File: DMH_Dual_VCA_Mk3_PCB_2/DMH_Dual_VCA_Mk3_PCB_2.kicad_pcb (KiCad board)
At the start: 2 copper layers, 48 x 175 mm, 78 parts, among them J1 TS_Jack_6.35mm_Sw, J100 IDC_02x05, J2 TS_Jack_6.35mm_Sw, J200 IDC_02x05, J3 TS_Jack_6.35mm_Sw, J4 TS_Jack_6.35mm_Sw, J5 TS_Jack_6.35mm_Sw, J50 Conn_01x08, J6 TS_Jack_6.35mm_Sw, J60 Conn_01x08, J7 TS_Jack_6.35mm_Sw, J8 TS_Jack_6.35mm_Sw, J9 TS_Jack_6.35mm_Sw, Q1 BC548, Q2 BC548, Q3 BC548, Q4 BC548, U1 TL074, U2 TL074, U3 TL072

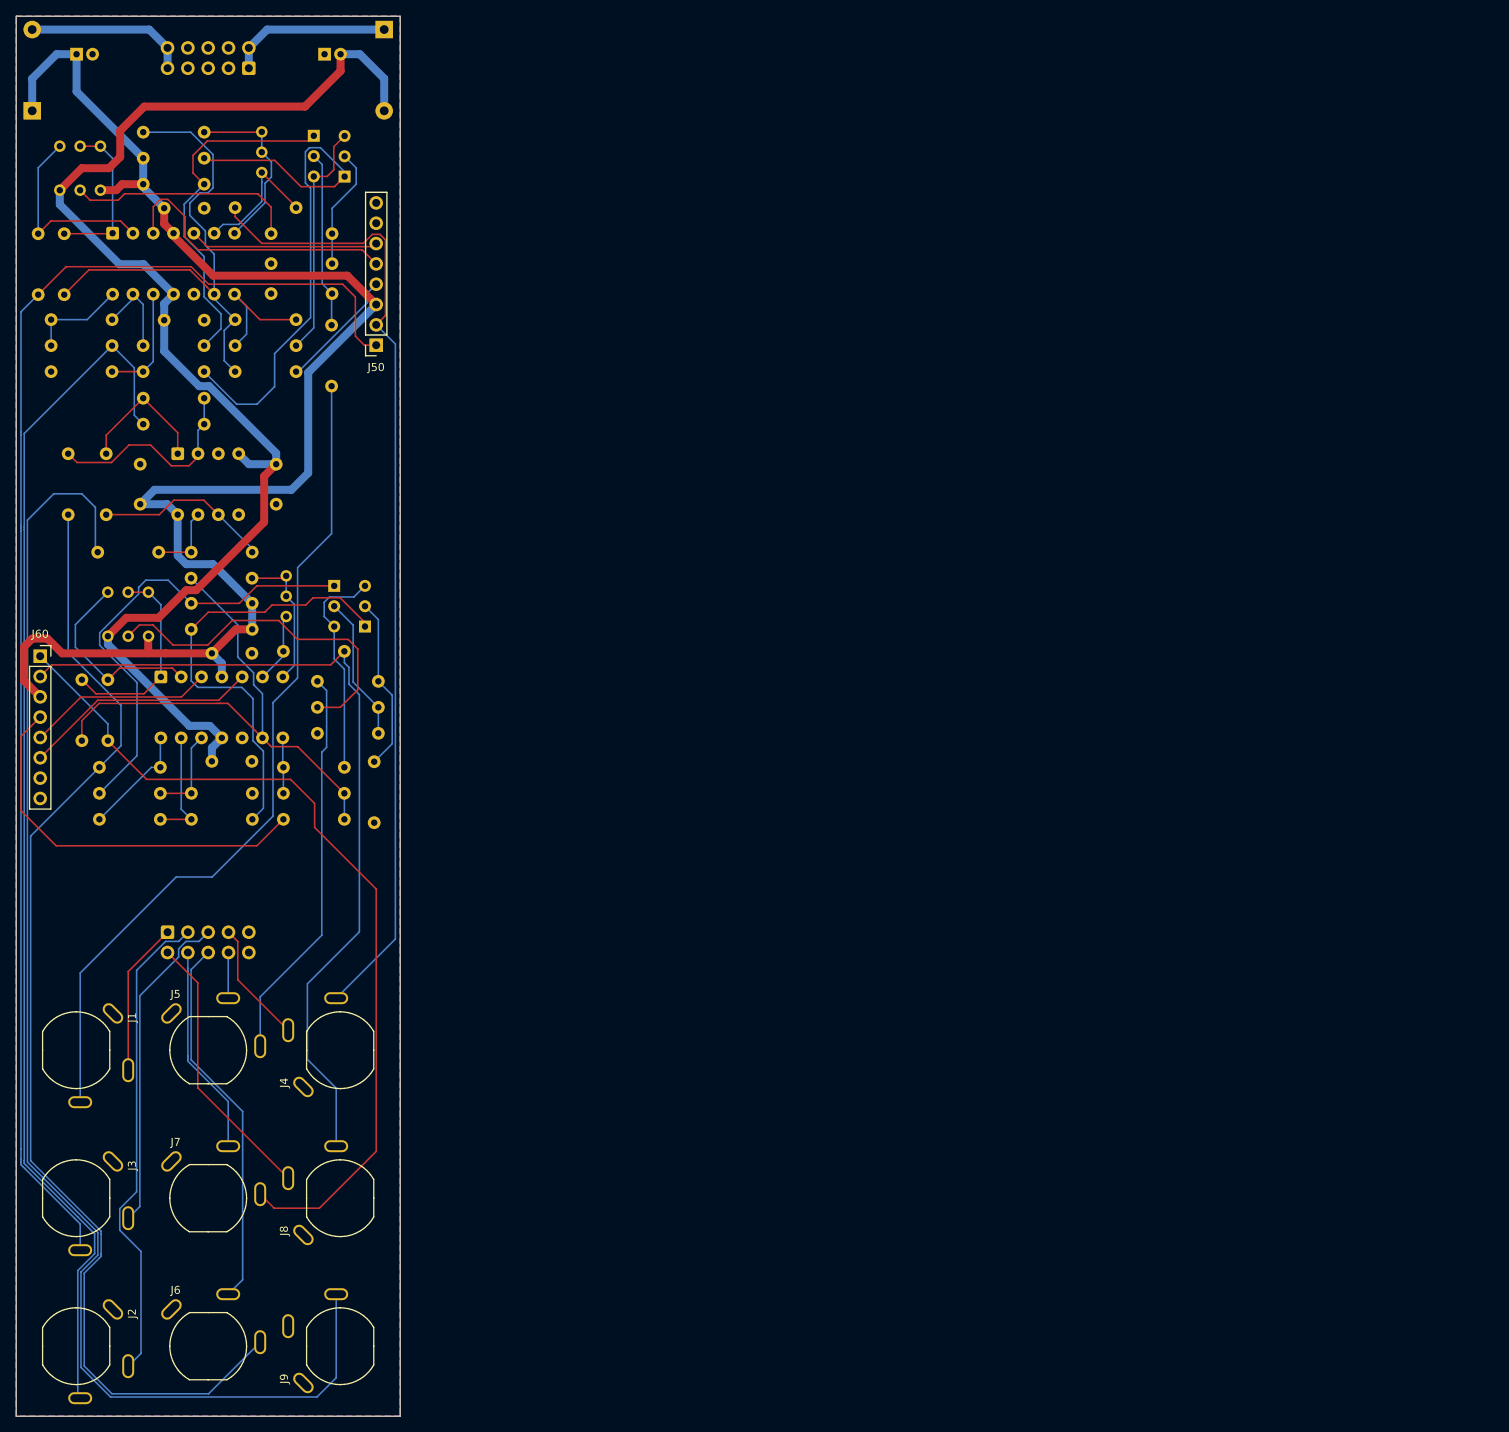
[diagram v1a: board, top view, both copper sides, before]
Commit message: Added clipping LED to schematic
Still need to add to Panel
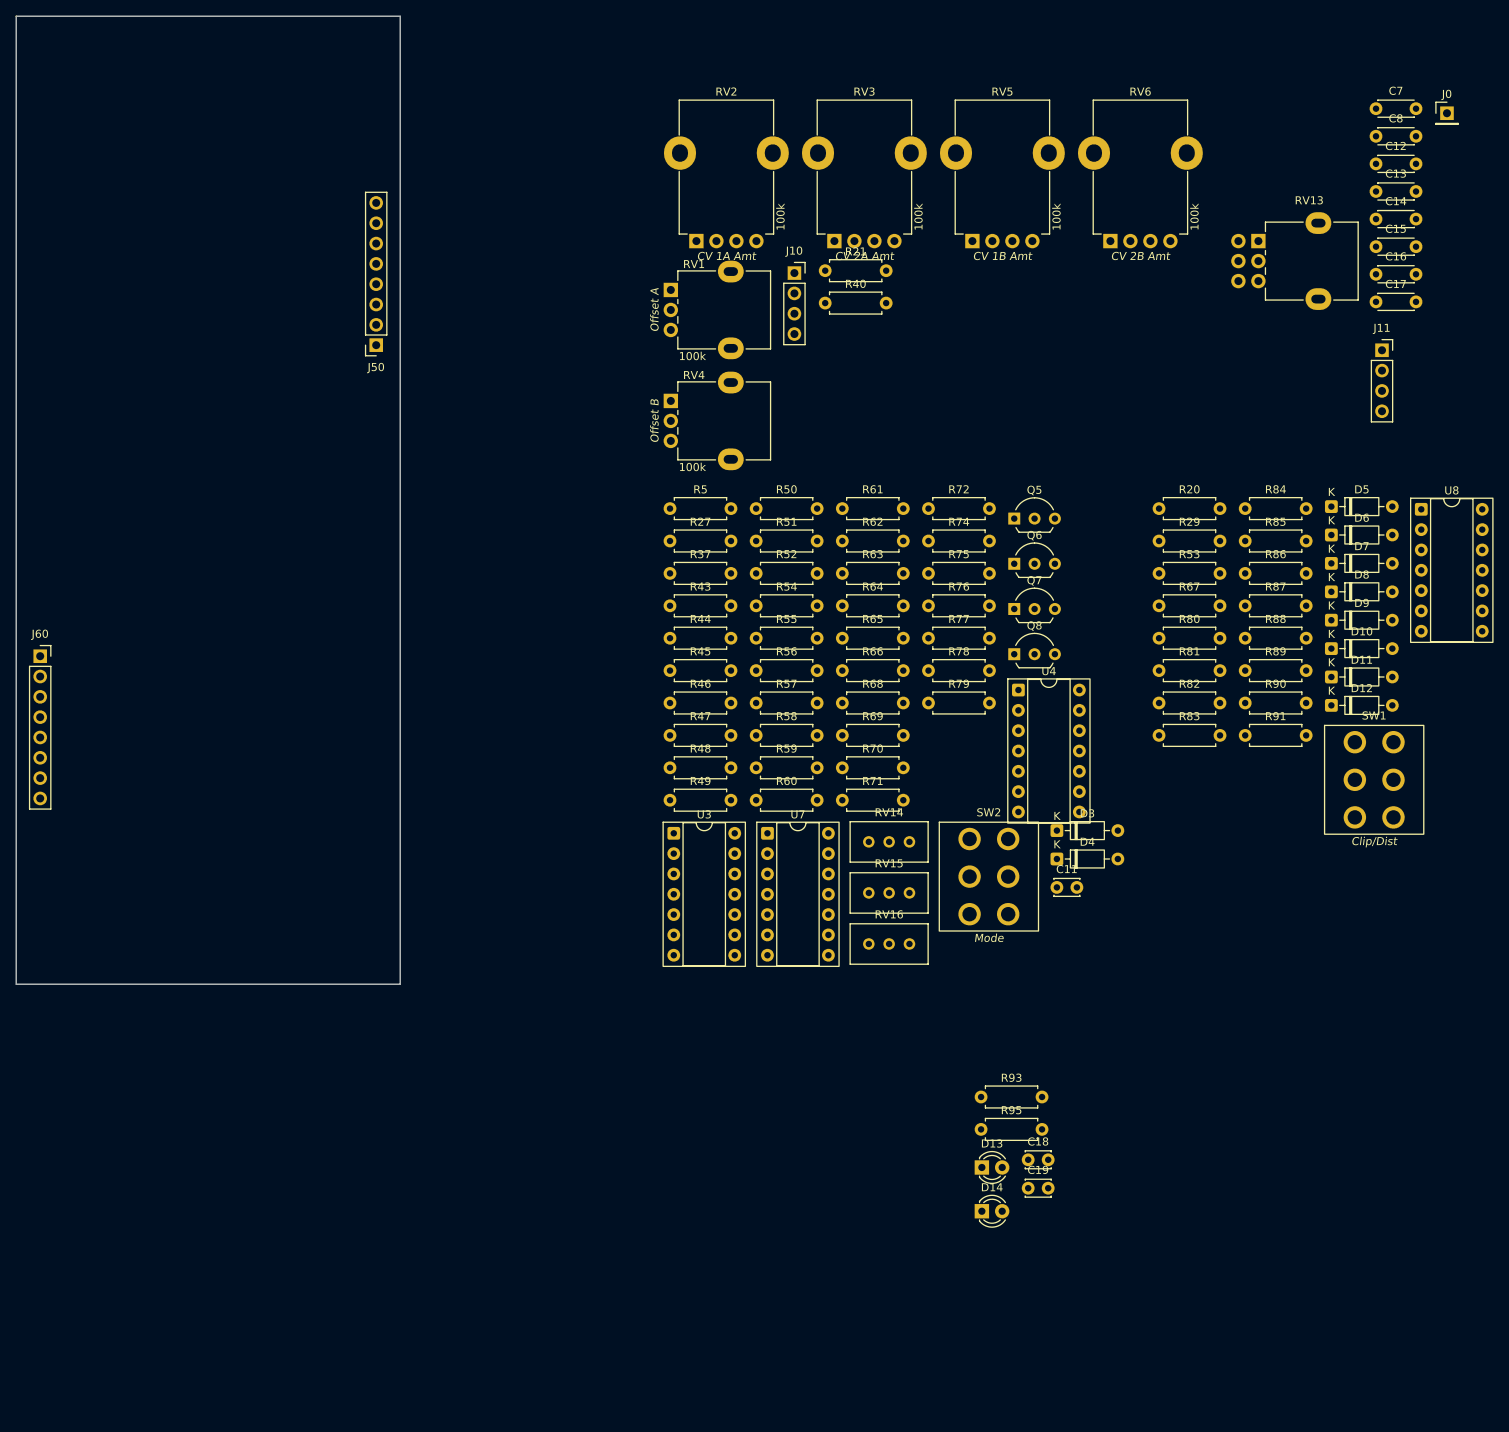
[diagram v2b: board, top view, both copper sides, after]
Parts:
- removed C1, C2: 47uF, Capacitor_THT:CP_Radial_D5.0mm_P2.00mm
- removed C3, C4, C5, C6: 100nF, Capacitor_THT:C_Disc_D4.3mm_W1.9mm_P5.00mm
- removed D1: SB140+, Diode_THT:D_DO-41_SOD81_P10.16mm_Horizontal
- removed D2: SB140-, Diode_THT:D_DO-41_SOD81_P10.16mm_Horizontal
- removed J1, J2, J3, J4, J5, J6, J7, J8, J9: TS_Jack_6.35mm_Sw, SynthStuff:CUI_MJ-63052A
- removed J100: IDC_02x05, SynthStuff:IDC-Header_2x05_P2.54mm_Vertical_Eurorack
- removed J200: IDC_02x05, SynthStuff:IDC-Header_2x05_P2.54mm_Vertical_BackBone
- removed Q1, Q2, Q3, Q4: BC548, Package_TO_SOT_THT:TO-92L_Inline_Wide
- removed R1, R24, R32, R4: 33k, Resistor_THT:R_Axial_DIN0207_L6.3mm_D2.5mm_P7.62mm_Horizontal
- removed R10, R13, R35, R36: 100R, Resistor_THT:R_Axial_DIN0207_L6.3mm_D2.5mm_P7.62mm_Horizontal
- removed R11, R12, R18, R19, R25, R28, R3, R31, R33, R34, R38, R41, R42, R6, R7, R8: 100k, Resistor_THT:R_Axial_DIN0207_L6.3mm_D2.5mm_P7.62mm_Horizontal
- removed R14, R15, R22, R23: 20k, Resistor_THT:R_Axial_DIN0207_L6.3mm_D2.5mm_P7.62mm_Horizontal
- removed R16, R17, R26, R30, R39, R9: 10k, Resistor_THT:R_Axial_DIN0207_L6.3mm_D2.5mm_P7.62mm_Horizontal
- removed RV10, RV11, RV12, RV9: 50k, Potentiometer_THT:Potentiometer_Bourns_3296W_Vertical
- removed RV7, RV8: 100k, Potentiometer_THT:Potentiometer_Bourns_3296W_Vertical
- removed U1, U2: TL074, Package_DIP:DIP-14_W7.62mm_Socket
- added C11: 22pF, Capacitor_THT:C_Disc_D3.0mm_W2.0mm_P2.50mm, F.Cu at (181.1, 151.4)
- added C12: 100nF, Capacitor_THT:C_Disc_D4.3mm_W1.9mm_P5.00mm, F.Cu at (221.0, 61.0)
- added C13: 100nF, Capacitor_THT:C_Disc_D4.3mm_W1.9mm_P5.00mm, F.Cu at (221.0, 64.4)
- added C14: 100nF, Capacitor_THT:C_Disc_D4.3mm_W1.9mm_P5.00mm, F.Cu at (221.0, 67.9)
- added C15: 100nF, Capacitor_THT:C_Disc_D4.3mm_W1.9mm_P5.00mm, F.Cu at (221.0, 71.3)
- added C16: 100nF, Capacitor_THT:C_Disc_D4.3mm_W1.9mm_P5.00mm, F.Cu at (221.0, 74.8)
- added C17: 100nF, Capacitor_THT:C_Disc_D4.3mm_W1.9mm_P5.00mm, F.Cu at (221.0, 78.2)
- added C18: 100pF, Capacitor_THT:C_Disc_D3.0mm_W2.0mm_P2.50mm, F.Cu at (177.5, 185.4)
- added C19: 100pF, Capacitor_THT:C_Disc_D3.0mm_W2.0mm_P2.50mm, F.Cu at (177.5, 189.0)
- added D10: ZPD3V0, Diode_THT:D_DO-35_SOD27_P7.62mm_Horizontal, F.Cu at (215.4, 121.5)
- added D11: ZPD3V0, Diode_THT:D_DO-35_SOD27_P7.62mm_Horizontal, F.Cu at (215.4, 125.1)
- added D12: ZPD3V0, Diode_THT:D_DO-35_SOD27_P7.62mm_Horizontal, F.Cu at (215.4, 128.7)
- added D13: LED_R, LED_THT:LED_D3.0mm, F.Cu at (171.7, 186.4)
- added D14: LED_R, LED_THT:LED_D3.0mm, F.Cu at (171.7, 191.9)
- added D3: 1N4148, Diode_THT:D_DO-35_SOD27_P7.62mm_Horizontal, F.Cu at (181.1, 144.3)
- added D4: 1N4148, Diode_THT:D_DO-35_SOD27_P7.62mm_Horizontal, F.Cu at (181.1, 147.8)
- added D5: ZPD4V7, Diode_THT:D_DO-35_SOD27_P7.62mm_Horizontal, F.Cu at (215.4, 103.8)
- added D6: ZPD4V7, Diode_THT:D_DO-35_SOD27_P7.62mm_Horizontal, F.Cu at (215.4, 107.3)
- added D7: ZPD4V7, Diode_THT:D_DO-35_SOD27_P7.62mm_Horizontal, F.Cu at (215.4, 110.9)
- added D8: ZPD4V7, Diode_THT:D_DO-35_SOD27_P7.62mm_Horizontal, F.Cu at (215.4, 114.5)
- added D9: ZPD3V0, Diode_THT:D_DO-35_SOD27_P7.62mm_Horizontal, F.Cu at (215.4, 118.0)
- added J0: Conn_01x01, Connector_PinHeader_2.54mm:PinHeader_1x01_P2.54mm_Vertical, F.Cu at (229.8, 54.6)
- added J10: Conn_01x04, Connector_PinSocket_2.54mm:PinSocket_1x04_P2.54mm_Vertical, F.Cu at (148.3, 74.6)
- added J11: Conn_01x04_PinHeader, Connector_PinSocket_2.54mm:PinSocket_1x04_P2.54mm_Vertical, F.Cu at (221.7, 84.3)
- added Q5: BC548, Package_TO_SOT_THT:TO-92L_Inline_Wide, F.Cu at (175.8, 105.3)
- added Q6: BC548, Package_TO_SOT_THT:TO-92L_Inline_Wide, F.Cu at (175.8, 111.0)
- added Q7: BC548, Package_TO_SOT_THT:TO-92L_Inline_Wide, F.Cu at (175.8, 116.6)
- added Q8: BC548, Package_TO_SOT_THT:TO-92L_Inline_Wide, F.Cu at (175.8, 122.2)
- added R21: 18k, Resistor_THT:R_Axial_DIN0207_L6.3mm_D2.5mm_P7.62mm_Horizontal, F.Cu at (152.1, 74.3)
- added R27: 100k, Resistor_THT:R_Axial_DIN0207_L6.3mm_D2.5mm_P7.62mm_Horizontal, F.Cu at (132.7, 108.1)
- added R37: 100k, Resistor_THT:R_Axial_DIN0207_L6.3mm_D2.5mm_P7.62mm_Horizontal, F.Cu at (132.7, 112.2)
- added R40: 18k, Resistor_THT:R_Axial_DIN0207_L6.3mm_D2.5mm_P7.62mm_Horizontal, F.Cu at (152.1, 78.4)
- added R43: 100R, Resistor_THT:R_Axial_DIN0207_L6.3mm_D2.5mm_P7.62mm_Horizontal, F.Cu at (132.7, 116.2)
- added R44: 20k, Resistor_THT:R_Axial_DIN0207_L6.3mm_D2.5mm_P7.62mm_Horizontal, F.Cu at (132.7, 120.2)
- added R45: 10k, Resistor_THT:R_Axial_DIN0207_L6.3mm_D2.5mm_P7.62mm_Horizontal, F.Cu at (132.7, 124.3)
- added R5: 100k, Resistor_THT:R_Axial_DIN0207_L6.3mm_D2.5mm_P7.62mm_Horizontal, F.Cu at (132.7, 104.0)
- added R52: 100k, Resistor_THT:R_Axial_DIN0207_L6.3mm_D2.5mm_P7.62mm_Horizontal, F.Cu at (143.5, 112.2)
- added R53: 20k, Resistor_THT:R_Axial_DIN0207_L6.3mm_D2.5mm_P7.62mm_Horizontal, F.Cu at (193.9, 112.2)
- added R54: 100k, Resistor_THT:R_Axial_DIN0207_L6.3mm_D2.5mm_P7.62mm_Horizontal, F.Cu at (143.5, 116.2)
- added R55: 100k, Resistor_THT:R_Axial_DIN0207_L6.3mm_D2.5mm_P7.62mm_Horizontal, F.Cu at (143.5, 120.2)
- added R56: 100k, Resistor_THT:R_Axial_DIN0207_L6.3mm_D2.5mm_P7.62mm_Horizontal, F.Cu at (143.5, 124.3)
- added R57: 100R, Resistor_THT:R_Axial_DIN0207_L6.3mm_D2.5mm_P7.62mm_Horizontal, F.Cu at (143.5, 128.3)
- added R58: 20k, Resistor_THT:R_Axial_DIN0207_L6.3mm_D2.5mm_P7.62mm_Horizontal, F.Cu at (143.5, 132.4)
- added R59: 10k, Resistor_THT:R_Axial_DIN0207_L6.3mm_D2.5mm_P7.62mm_Horizontal, F.Cu at (143.5, 136.4)
- added R60: 20k, Resistor_THT:R_Axial_DIN0207_L6.3mm_D2.5mm_P7.62mm_Horizontal, F.Cu at (143.5, 140.5)
- added R61: 10k, Resistor_THT:R_Axial_DIN0207_L6.3mm_D2.5mm_P7.62mm_Horizontal, F.Cu at (154.3, 104.0)
- added R62: 10k, Resistor_THT:R_Axial_DIN0207_L6.3mm_D2.5mm_P7.62mm_Horizontal, F.Cu at (154.3, 108.1)
- added R63: 100R, Resistor_THT:R_Axial_DIN0207_L6.3mm_D2.5mm_P7.62mm_Horizontal, F.Cu at (154.3, 112.2)
- added R64: 100k, Resistor_THT:R_Axial_DIN0207_L6.3mm_D2.5mm_P7.62mm_Horizontal, F.Cu at (154.3, 116.2)
- added R65: 100k, Resistor_THT:R_Axial_DIN0207_L6.3mm_D2.5mm_P7.62mm_Horizontal, F.Cu at (154.3, 120.2)
- added R66: 100k, Resistor_THT:R_Axial_DIN0207_L6.3mm_D2.5mm_P7.62mm_Horizontal, F.Cu at (154.3, 124.3)
- added R67: 20k, Resistor_THT:R_Axial_DIN0207_L6.3mm_D2.5mm_P7.62mm_Horizontal, F.Cu at (193.9, 116.2)
- added R68: 33k, Resistor_THT:R_Axial_DIN0207_L6.3mm_D2.5mm_P7.62mm_Horizontal, F.Cu at (154.3, 128.3)
- added R69: 100k, Resistor_THT:R_Axial_DIN0207_L6.3mm_D2.5mm_P7.62mm_Horizontal, F.Cu at (154.3, 132.4)
- added R70: 100k, Resistor_THT:R_Axial_DIN0207_L6.3mm_D2.5mm_P7.62mm_Horizontal, F.Cu at (154.3, 136.4)
- added R71: 100k, Resistor_THT:R_Axial_DIN0207_L6.3mm_D2.5mm_P7.62mm_Horizontal, F.Cu at (154.3, 140.5)
- added R72: 100k, Resistor_THT:R_Axial_DIN0207_L6.3mm_D2.5mm_P7.62mm_Horizontal, F.Cu at (165.0, 104.0)
- added R74: 100k, Resistor_THT:R_Axial_DIN0207_L6.3mm_D2.5mm_P7.62mm_Horizontal, F.Cu at (165.0, 108.1)
- added R75: 100k, Resistor_THT:R_Axial_DIN0207_L6.3mm_D2.5mm_P7.62mm_Horizontal, F.Cu at (165.0, 112.2)
- added R76: 100k, Resistor_THT:R_Axial_DIN0207_L6.3mm_D2.5mm_P7.62mm_Horizontal, F.Cu at (165.0, 116.2)
- added R77: 20k, Resistor_THT:R_Axial_DIN0207_L6.3mm_D2.5mm_P7.62mm_Horizontal, F.Cu at (165.0, 120.2)
- added R78: 20k, Resistor_THT:R_Axial_DIN0207_L6.3mm_D2.5mm_P7.62mm_Horizontal, F.Cu at (165.0, 124.3)
- added R79: 10k, Resistor_THT:R_Axial_DIN0207_L6.3mm_D2.5mm_P7.62mm_Horizontal, F.Cu at (165.0, 128.3)
- added R80: 100k, Resistor_THT:R_Axial_DIN0207_L6.3mm_D2.5mm_P7.62mm_Horizontal, F.Cu at (193.9, 120.2)
- added R81: 100k, Resistor_THT:R_Axial_DIN0207_L6.3mm_D2.5mm_P7.62mm_Horizontal, F.Cu at (193.9, 124.3)
- added R82: 220k, Resistor_THT:R_Axial_DIN0207_L6.3mm_D2.5mm_P7.62mm_Horizontal, F.Cu at (193.9, 128.3)
- added R83: 20k, Resistor_THT:R_Axial_DIN0207_L6.3mm_D2.5mm_P7.62mm_Horizontal, F.Cu at (193.9, 132.4)
- added R84: 2k2, Resistor_THT:R_Axial_DIN0207_L6.3mm_D2.5mm_P7.62mm_Horizontal, F.Cu at (204.6, 104.0)
- added R85: 100k, Resistor_THT:R_Axial_DIN0207_L6.3mm_D2.5mm_P7.62mm_Horizontal, F.Cu at (204.6, 108.1)
- added R86: 220k, Resistor_THT:R_Axial_DIN0207_L6.3mm_D2.5mm_P7.62mm_Horizontal, F.Cu at (204.6, 112.2)
- added R87: 100k, Resistor_THT:R_Axial_DIN0207_L6.3mm_D2.5mm_P7.62mm_Horizontal, F.Cu at (204.6, 116.2)
- added R88: 2k2, Resistor_THT:R_Axial_DIN0207_L6.3mm_D2.5mm_P7.62mm_Horizontal, F.Cu at (204.6, 120.2)
- added R89: 2k2, Resistor_THT:R_Axial_DIN0207_L6.3mm_D2.5mm_P7.62mm_Horizontal, F.Cu at (204.6, 124.3)
- added R90: 1k, Resistor_THT:R_Axial_DIN0207_L6.3mm_D2.5mm_P7.62mm_Horizontal, F.Cu at (204.6, 128.3)
- added R91: 1k, Resistor_THT:R_Axial_DIN0207_L6.3mm_D2.5mm_P7.62mm_Horizontal, F.Cu at (204.6, 132.4)
- added R93: 2k2, Resistor_THT:R_Axial_DIN0207_L6.3mm_D2.5mm_P7.62mm_Horizontal, F.Cu at (171.6, 177.6)
- added R95: 2k2, Resistor_THT:R_Axial_DIN0207_L6.3mm_D2.5mm_P7.62mm_Horizontal, F.Cu at (171.6, 181.7)
- added RV1: 100k, SynthStuff:Potentiometer_Alpha_RD901F-40-00D_Single_Vertical, F.Cu at (132.8, 76.7)
- added RV13: 100k, Potentiometer_THT:Potentiometer_Alpha_RD902F-40-00D_Dual_Vertical, F.Cu at (206.3, 70.6)
- added RV14: 100k, Potentiometer_THT:Potentiometer_Bourns_3296W_Vertical, F.Cu at (162.7, 145.7)
- added RV15: 100k, Potentiometer_THT:Potentiometer_Bourns_3296W_Vertical, F.Cu at (162.7, 152.1)
- added RV16: 50k, Potentiometer_THT:Potentiometer_Bourns_3296W_Vertical, F.Cu at (162.7, 158.5)
- added RV2: 100k, SynthStuff:Potentiometer_TT_P110KH1, F.Cu at (137.3, 70.6)
- added RV3: 100k, SynthStuff:Potentiometer_TT_P110KH1, F.Cu at (154.5, 70.6)
- added RV4: 100k, SynthStuff:Potentiometer_Alpha_RD901F-40-00D_Single_Vertical, F.Cu at (132.8, 90.6)
- added RV5: 100k, SynthStuff:Potentiometer_TT_P110KH1, F.Cu at (171.8, 70.6)
- added RV6: 100k, SynthStuff:Potentiometer_TT_P110KH1, F.Cu at (189.0, 70.6)
- added SW1: SW_DPDT_OnOffOn_x2, SynthStuff:Toggle_Switch_2_Poles_TE, F.Cu at (220.7, 137.9)
- added SW2: SW_DPDT_3way, SynthStuff:Toggle_Switch_2_Poles_TE, F.Cu at (172.6, 150.1)
- added U4: TL074, Package_DIP:DIP-14_W7.62mm_Socket, F.Cu at (176.3, 126.7)
- added U7: TL074, Package_DIP:DIP-14_W7.62mm_Socket, F.Cu at (144.9, 144.6)
- added U8: TL074, Package_DIP:DIP-14_W7.62mm_Socket, F.Cu at (226.6, 104.1)
- C7, C8, R50: moved to F.Cu
- R20: value 1k -> 2k2; moved to F.Cu
- R29: value 1k -> 20k; moved to F.Cu
- R46: value 100k -> 20k; moved to F.Cu
- R47: value 100k -> 100R; moved to F.Cu
- R48, R49: value 100k -> 10k; moved to F.Cu
- R51: value 1k -> 100k; moved to F.Cu
- U3: value TL072 -> TL074; footprint Package_DIP:DIP-8_W7.62mm_Socket -> Package_DIP:DIP-14_W7.62mm_Socket; moved to F.Cu
- moved C7 162.2 mm to (221.0, 54.1), turned to 0 degrees
- moved C8 145.0 mm to (221.0, 57.5), turned to 0 degrees
- moved R29 135.4 mm to (193.9, 108.1)
- moved R20 132.4 mm to (193.9, 104.0), turned to 0 degrees
- moved R49 82.7 mm to (132.7, 140.5), turned to 0 degrees
- moved R46 78.8 mm to (132.7, 128.3), turned to 0 degrees
- moved R48 78.6 mm to (132.7, 136.4)
- moved U3 78.1 mm to (133.2, 144.6), turned to 0 degrees
- moved R51 74.7 mm to (143.5, 108.1), turned to 0 degrees
- moved R47 71.9 mm to (132.7, 132.4), turned to 0 degrees
- moved R50 63.2 mm to (143.5, 104.0), turned to 0 degrees
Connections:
- J50 pad 1: /Core Circuit A/CV 1 A Input -> /Inputs and Outputs/CV 1 A Jack
- J50 pad 2: /Core Circuit A/CV 2 A Input -> /Inputs and Outputs/CV 2 A Jack
- J50 pad 4: /Core Circuit A/Offset A Pot -> /Inputs and Outputs/Offset A Pot
- J50 pad 5: /Core Circuit A/CV 1 A Pot -> /Inputs and Outputs/CV 1 A Pot
- J50 pad 6: /Core Circuit A/CV 2 A Pot -> /Inputs and Outputs/CV 2 A Pot
- J50 pad 7: GND -> -12V
- J60 pad 1: /Core Circuit B/CV 1 B Input -> /Inputs and Outputs/CV 1 B Jack
- J60 pad 2: /Core Circuit B/CV 2 B Input -> /Inputs and Outputs/CV 2 B Jack
- J60 pad 4: /Core Circuit B/Offset B Pot -> /Inputs and Outputs/Offset B Pot
- J60 pad 5: /Core Circuit B/CV 1 B Pot -> /Inputs and Outputs/CV 1 B Pot
- J60 pad 6: /Core Circuit B/CV 2 B Pot -> /Inputs and Outputs/CV 2 B Pot
- J60 pad 7: GND -> -12V
- R20 pad 1: /Core Circuit A/Output A -> Net-(R20-Pad1)
- R29 pad 1: /Core Circuit B/Output B -> /2nd VCA/Output B
- R46 pad 1: /Core Circuit B/Output B -> Net-(Q6-C)
- R46 pad 2: Net-(U3A--) -> +12V
- R47 pad 1: Net-(U3A--) -> GND
- R47 pad 2: Net-(R47-Pad2) -> Net-(Q6-B)
- R48 pad 1: /Core Circuit A/Output A -> Net-(U3C--)
- R48 pad 2: Net-(U3A--) -> Net-(Q5-C)
- R49 pad 1: Net-(R47-Pad2) -> Net-(U3C-+)
- R49 pad 2: Net-(U3B--) -> Net-(Q6-C)
- R50 pad 1: Net-(U3B--) -> Net-(R50-Pad1)
- R50 pad 2: Net-(R50-Pad2) -> Net-(Q6-B)
- R51 pad 1: Net-(R50-Pad2) -> Net-(U3C-+)
- R51 pad 2: /Inputs and Outputs/Mix Out Jack -> GND
- U3 pad 1: Net-(R47-Pad2) -> Net-(R27-Pad2)
- U3 pad 4: -12V -> +12V
- U3 pad 5: GND -> Net-(U3B-+)
- U3 pad 7: Net-(R50-Pad2) -> /2nd VCA/Output B
- U3 pad 8: +12V -> /2nd VCA/Output A
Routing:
- net +12V: track 189.3 -> 0.00 mm
- net /Core Circuit A/CV 1 A Input: track 174.0 -> 0.00 mm
- net /Inputs and Outputs/Mix Out Jack: track 171.6 -> 0.00 mm
- net -12V: track 167.1 -> 0.00 mm
- net /Core Circuit A/Output A: track 152.2 -> 0.00 mm
- net /Core Circuit B/Output B: track 144.5 -> 0.00 mm
- net /Core Circuit A/CV 2 A Input: track 121.4 -> 0.00 mm
- net /Core Circuit B/CV 1 B Input: track 108.0 -> 0.00 mm
- net /Core Circuit B/CV 2 B Input: track 106.1 -> 0.00 mm
- net /Core Circuit A/Input A: track 105.2 -> 0.00 mm
- net Net-(Q2-C): track 69.4 -> 0.00 mm
- net Net-(U2C--): track 67.8 -> 0.00 mm
- net Net-(U1C--): track 63.6 -> 0.00 mm
- net Net-(J200-Pin_2): track 60.5 -> 0.00 mm
- net Net-(Q4-C): track 58.6 -> 0.00 mm
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- removed copper zone on B.Cu, net GND
- removed copper zone on F.Cu, net GND
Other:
- board size 48 x 175 mm -> 48 x 121 mm

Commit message: Positioned controls on PCB 2
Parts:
- removed J0: Conn_01x01, Connector_PinHeader_2.54mm:PinHeader_1x01_P2.54mm_Vertical
- added D15: 1N4148, Diode_THT:D_DO-35_SOD27_P7.62mm_Horizontal, F.Cu at (145.7, 176.2)
- added D16: LED_R, LED_THT:LED_D3.0mm, F.Cu at (86.0, 117.5)
- added R100: 20k, Resistor_THT:R_Axial_DIN0207_L6.3mm_D2.5mm_P7.62mm_Horizontal, F.Cu at (134.9, 200.7)
- added R101: 3k3, Resistor_THT:R_Axial_DIN0207_L6.3mm_D2.5mm_P7.62mm_Horizontal, F.Cu at (134.9, 204.8)
- added R92: 20k, Resistor_THT:R_Axial_DIN0207_L6.3mm_D2.5mm_P7.62mm_Horizontal, F.Cu at (134.9, 176.4)
- added R94: 100k, Resistor_THT:R_Axial_DIN0207_L6.3mm_D2.5mm_P7.62mm_Horizontal, F.Cu at (134.9, 180.4)
- added R96: 1k, Resistor_THT:R_Axial_DIN0207_L6.3mm_D2.5mm_P7.62mm_Horizontal, F.Cu at (134.9, 184.5)
- added R97: 330k, Resistor_THT:R_Axial_DIN0207_L6.3mm_D2.5mm_P7.62mm_Horizontal, F.Cu at (134.9, 188.6)
- added R98: 330k, Resistor_THT:R_Axial_DIN0207_L6.3mm_D2.5mm_P7.62mm_Horizontal, F.Cu at (134.9, 192.6)
- added R99: 100k, Resistor_THT:R_Axial_DIN0207_L6.3mm_D2.5mm_P7.62mm_Horizontal, F.Cu at (134.9, 196.7)
- C18, C19: value 100pF -> 2.2uF; footprint Capacitor_THT:C_Disc_D3.0mm_W2.0mm_P2.50mm -> Capacitor_THT:CP_Radial_D4.0mm_P1.50mm
- D14: value LED_R -> 1N4148; footprint LED_THT:LED_D3.0mm -> Diode_THT:D_DO-35_SOD27_P7.62mm_Horizontal
- R29, R53, R67, R83: value 20k -> 100k
- R93: value 2k2 -> 3k3
- R95: value 2k2 -> 1k
- RV13: value 100k -> 50k; footprint Potentiometer_THT:Potentiometer_Alpha_RD902F-40-00D_Dual_Vertical -> Potentiometer_THT:Potentiometer_Alps_RK09L_Double_Vertical
- moved RV6 156.8 mm to (60.2, 160.0)
- moved SW1 145.6 mm to (87.2, 79.8)
- moved D13 129.8 mm to (86.0, 89.0)
- moved RV13 128.8 mm to (84.8, 113.2), turned to 90 degrees
- moved RV5 126.4 mm to (60.2, 130.0)
- moved RV3 97.9 mm to (60.2, 97.0)
- moved SW2 88.5 mm to (87.2, 126.8)
- moved RV4 81.6 mm to (84.8, 156.5), turned to 90 degrees
- moved RV2 77.1 mm to (60.2, 67.0)
- moved RV1 49.9 mm to (84.8, 63.5), turned to 90 degrees
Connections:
- C18 pad 1: Net-(U4C-+) -> Net-(D15-K)
- C18 pad 2: Net-(C18-Pad2) -> GND
- C19 pad 1: Net-(U4D-+) -> Net-(D14-K)
- C19 pad 2: Net-(C19-Pad2) -> GND
- D14 pad 1: GND -> Net-(D14-K)
- R29 pad 2: Net-(U4D-+) -> Net-(U8D--)
- R53 pad 2: Net-(U4C-+) -> Net-(U8A--)
- R67 pad 2: Net-(U4C-+) -> Net-(U8A--)
- R83 pad 2: Net-(U4D-+) -> Net-(U8D--)
- R93 pad 1: Net-(C18-Pad2) -> Net-(R93-Pad1)
- R95 pad 1: Net-(C19-Pad2) -> Net-(D14-A)
- R95 pad 2: Net-(D14-A) -> /2nd VCA/Output B
- U4 pad 10: Net-(U4C-+) -> Net-(D15-K)
- U4 pad 12: Net-(U4D-+) -> Net-(D14-K)
- U4 pad 13: +5V -> Net-(U4D--)
- U4 pad 14: Net-(C19-Pad2) -> Net-(R101-Pad1)
- U4 pad 8: Net-(C18-Pad2) -> Net-(R93-Pad1)
- U4 pad 9: +5V -> Net-(U4C--)
- U8 pad 13: Net-(U4D-+) -> Net-(U8D--)
- U8 pad 2: Net-(U4C-+) -> Net-(U8A--)
